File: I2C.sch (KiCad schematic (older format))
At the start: 2 parts, among them U1 PCA9306DP

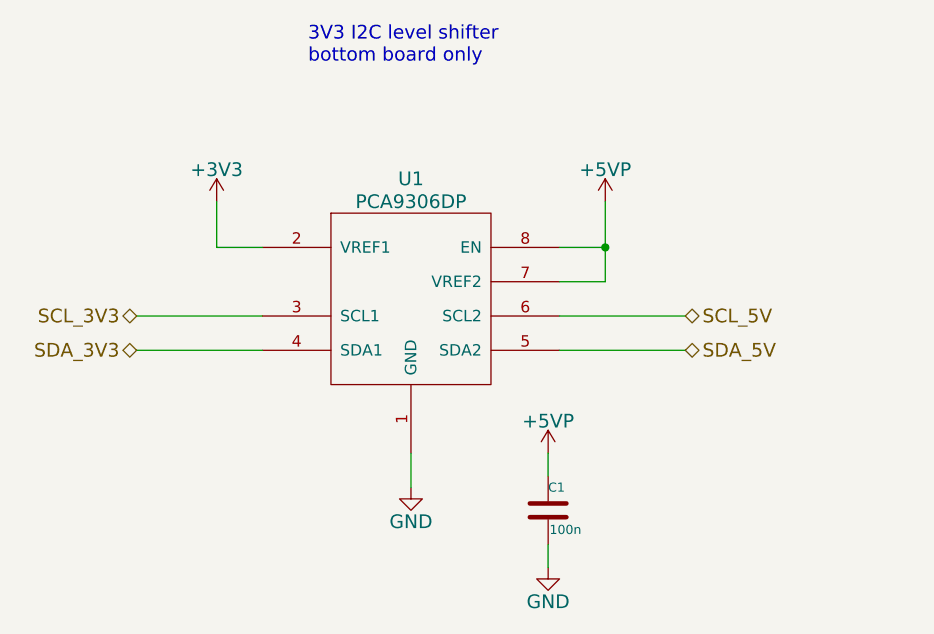
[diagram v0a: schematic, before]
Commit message: Added pullup resistors to I2C
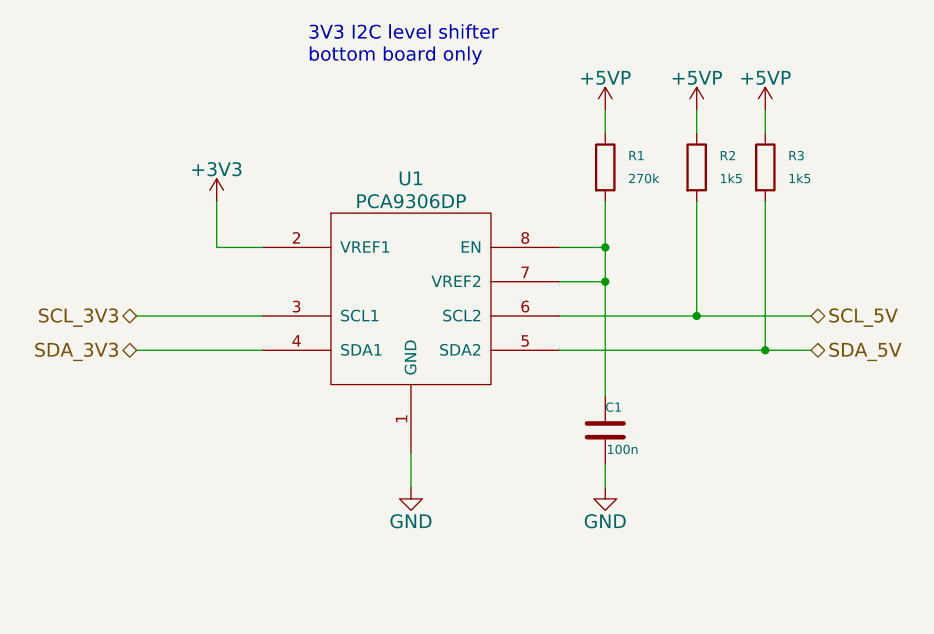
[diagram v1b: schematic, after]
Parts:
- added R1: 270k, Resistors_SMD:R_0805, symbol R
- added R2, R3: 1k5, Resistors_SMD:R_0805, symbol R
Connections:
- net +5VP: now also R1.1, R2.1, R3.1; no longer C1.1, U1.7 (VREF2), U1.8 (EN)
- net SCL_5V: now also R2.2
- net SDA_5V: now also R3.2
- new net: C1.1, R1.2, U1.7 (VREF2), U1.8 (EN)
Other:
- moved on the sheet: C1
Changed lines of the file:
@@
 	4000 2500 4000 2300
 $Comp
-L +3V3 #PWR010
+L +3V3 #PWR10
 U 1 1 54D96007
 P 4000 2300
-F 0 "#PWR010" H 4000 2150 60  0001 C CNN
+F 0 "#PWR10" H 4000 2150 60  0001 C CNN
 F 1 "+3V3" H 4000 2440 60  0000 C CNN
 F 2 "" H 4000 2300 60  0000 C CNN
@@
 	5700 2650 5500 2650
 Wire Wire Line
-	5700 2300 5700 2650
-Wire Wire Line
 	5500 2500 5700 2500
-Connection ~ 5700 2500
 $Comp
-L +5VP #PWR011
+L +5VP #PWR14
 U 1 1 54D96030
-P 5700 2300
-F 0 "#PWR011" H 5700 2150 60  0001 C CNN
-F 1 "+5VP" H 5700 2440 60  0000 C CNN
-F 2 "" H 5700 2300 60  0000 C CNN
-F 3 "" H 5700 2300 60  0000 C CNN
-	1    5700 2300
+P 6100 1900
+F 0 "#PWR14" H 6100 1750 60  0001 C CNN
+F 1 "+5VP" H 6100 2040 60  0000 C CNN
+F 2 "" H 6100 1900 60  0000 C CNN
+F 3 "" H 6100 1900 60  0000 C CNN
+	1    6100 1900
 	1    0    0    -1
 $EndComp
@@
 	4850 3400 4850 3550
 $Comp
-L GND #PWR012
+L GND #PWR11
 U 1 1 54D96055
 P 4850 3550
-F 0 "#PWR012" H 4850 3300 60  0001 C CNN
+F 0 "#PWR11" H 4850 3300 60  0001 C CNN
 F 1 "GND" H 4850 3400 60  0000 C CNN
 F 2 "" H 4850 3550 60  0000 C CNN
@@
 $EndComp
 $Comp
-L GND #PWR013
+L GND #PWR13
 U 1 1 54D9606F
-P 5450 3900
-F 0 "#PWR013" H 5450 3650 60  0001 C CNN
-F 1 "GND" H 5450 3750 60  0000 C CNN
-F 2 "" H 5450 3900 60  0000 C CNN
-F 3 "" H 5450 3900 60  0000 C CNN
-	1    5450 3900
+P 5700 3550
+F 0 "#PWR13" H 5700 3300 60  0001 C CNN
+F 1 "GND" H 5700 3400 60  0000 C CNN
+F 2 "" H 5700 3550 60  0000 C CNN
+F 3 "" H 5700 3550 60  0000 C CNN
+	1    5700 3550
 	1    0    0    -1
 $EndComp
@@
 L C C1
 U 1 1 54D96092
-P 5450 3650
-F 0 "C1" H 5450 3750 40  0000 L CNN
-F 1 "100n" H 5456 3565 40  0000 L CNN
-F 2 "Capacitors_SMD:C_0805" H 5488 3500 30  0001 C CNN
-F 3 "" H 5450 3650 60  0000 C CNN
-F 4 "MC0805B104K250CT" H 5450 3650 60  0001 C CNN "Part Number"
-F 5 "Multicomp" H 5450 3650 60  0001 C CNN "Manufacturer"
-F 6 "0805" H 5450 3650 60  0001 C CNN "Package"
-F 7 "Farnell" H 5450 3650 60  0001 C CNN "Supplier"
-F 8 "1759166" H 5450 3650 60  0001 C CNN "Order Code"
-F 9 "Mouser" H 5450 3650 60  0001 C CNN "Alt. Supplier"
-F 10 "710-885012207098" H 5450 3650 60  0001 C CNN "Alt. Order Code"
-F 11 "100nF/50V X7R 0805 ceramic capacitor" H 5450 3650 60  0001 C CNN "Note"
-	1    5450 3650
+P 5700 3300
+F 0 "C1" H 5700 3400 40  0000 L CNN
+F 1 "100n" H 5706 3215 40  0000 L CNN
+F 2 "Capacitors_SMD:C_0805" H 5738 3150 30  0001 C CNN
+F 3 "" H 5700 3300 60  0000 C CNN
+F 4 "MC0805B104K250CT" H 5700 3300 60  0001 C CNN "Part Number"
+F 5 "Multicomp" H 5700 3300 60  0001 C CNN "Manufacturer"
+F 6 "0805" H 5700 3300 60  0001 C CNN "Package"
+F 7 "Farnell" H 5700 3300 60  0001 C CNN "Supplier"
+F 8 "1759166" H 5700 3300 60  0001 C CNN "Order Code"
+F 9 "Mouser" H 5700 3300 60  0001 C CNN "Alt. Supplier"
+F 10 "710-885012207098" H 5700 3300 60  0001 C CNN "Alt. Order Code"
+F 11 "100nF/50V X7R 0805 ceramic capacitor" H 5700 3300 60  0001 C CNN "Note"
+	1    5700 3300
 	1    0    0    -1
 $EndComp
 Wire Wire Line
-	5450 3500 5450 3400
+	5700 3550 5700 3450
 Wire Wire Line
-	5450 3900 5450 3800
-$Comp
-L +5VP #PWR014
-U 1 1 54D960F9
-P 5450 3400
-F 0 "#PWR014" H 5450 3250 60  0001 C CNN
-F 1 "+5VP" H 5450 3540 60  0000 C CNN
-F 2 "" H 5450 3400 60  0000 C CNN
-F 3 "" H 5450 3400 60  0000 C CNN
-	1    5450 3400
-	1    0    0    -1
-$EndComp
+	5500 2800 6600 2800
 Wire Wire Line
-	5500 2800 6050 2800
-Wire Wire Line
-	5500 2950 6050 2950
+	5500 2950 6600 2950
 Wire Wire Line
 	4200 2800 3650 2800
@@
 Text HLabel 3650 2950 0    60   BiDi ~ 0
 SDA_3V3
-Text HLabel 6050 2800 2    60   BiDi ~ 0
+Text HLabel 6600 2800 2    60   BiDi ~ 0
 SCL_5V
-Text HLabel 6050 2950 2    60   BiDi ~ 0
+Text HLabel 6600 2950 2    60   BiDi ~ 0
 SDA_5V
 Text Notes 4400 1700 0    60   ~ 0
 3V3 I2C level shifter\nbottom board only
+$Comp
+L R R1
+U 1 1 56EC1C2A
+P 5700 2150
+F 0 "R1" H 5800 2200 40  0000 L CNN
+F 1 "270k" H 5800 2100 40  0000 L CNN
+F 2 "Resistors_SMD:R_0805" V 5630 2150 30  0001 C CNN
+F 3 "" H 5700 2150 30  0000 C CNN
+F 4 "MCSR08X2703FTL" V 5700 2150 60  0001 C CNN "Part Number"
+F 5 "Multicomp" V 5700 2150 60  0001 C CNN "Manufacturer"
+F 6 "0805" H 5700 2150 60  0001 C CNN "Package"
+F 7 "Farnell" H 5700 2150 60  0001 C CNN "Supplier"
+F 8 "2074426" V 5700 2150 60  0001 C CNN "Order Code"
+F 9 "Mouser" H 5700 2150 60  0001 C CNN "Alt. Supplier"
+F 10 "ERJ-6ENF2703V" H 5700 2150 60  0001 C CNN "Alt. Order Code"
+F 11 "270kΩ/1% 0805 resistor" H 5700 2150 60  0001 C CNN "Note"
+	1    5700 2150
+	1    0    0    -1
+$EndComp
+Wire Wire Line
+	6100 1900 6100 2000
+Wire Wire Line
+	5700 2300 5700 3150
+Connection ~ 5700 2500
+Connection ~ 5700 2650
+$Comp
+L R R2
+U 1 1 56EC20D7
+P 6100 2150
+F 0 "R2" H 6200 2200 40  0000 L CNN
+F 1 "1k5" H 6200 2100 40  0000 L CNN
+F 2 "Resistors_SMD:R_0805" V 6030 2150 30  0001 C CNN
+F 3 "" H 6100 2150 30  0000 C CNN
+F 4 "MCWR08X1501FTL" V 6100 2150 60  0001 C CNN "Part Number"
+F 5 "Multicomp" V 6100 2150 60  0001 C CNN "Manufacturer"
+F 6 "0805" H 6100 2150 60  0001 C CNN "Package"
+F 7 "Farnell" H 6100 2150 60  0001 C CNN "Supplier"
+F 8 "2447592" V 6100 2150 60  0001 C CNN "Order Code"
+F 9 "Mouser" H 6100 2150 60  0001 C CNN "Alt. Supplier"
+F 10 "71-CRCW0805-1.5K-E3" H 6100 2150 60  0001 C CNN "Alt. Order Code"
+F 11 "1.5kΩ/1% 0805 resistor" H 6100 2150 60  0001 C CNN "Note"
+	1    6100 2150
+	1    0    0    -1
+$EndComp
+$Comp
+L R R3
+U 1 1 56EC2261
+P 6400 2150
+F 0 "R3" H 6500 2200 40  0000 L CNN
+F 1 "1k5" H 6500 2100 40  0000 L CNN
+F 2 "Resistors_SMD:R_0805" V 6330 2150 30  0001 C CNN
+F 3 "" H 6400 2150 30  0000 C CNN
+F 4 "MCWR08X1501FTL" V 6400 2150 60  0001 C CNN "Part Number"
+F 5 "Multicomp" V 6400 2150 60  0001 C CNN "Manufacturer"
+F 6 "0805" H 6400 2150 60  0001 C CNN "Package"
+F 7 "Farnell" H 6400 2150 60  0001 C CNN "Supplier"
+F 8 "2447592" V 6400 2150 60  0001 C CNN "Order Code"
+F 9 "Mouser" H 6400 2150 60  0001 C CNN "Alt. Supplier"
+F 10 "71-CRCW0805-1.5K-E3" H 6400 2150 60  0001 C CNN "Alt. Order Code"
+F 11 "1.5kΩ/1% 0805 resistor" H 6400 2150 60  0001 C CNN "Note"
+	1    6400 2150
+	1    0    0    -1
+$EndComp
+Wire Wire Line
+	6100 2300 6100 2800
+Connection ~ 6100 2800
+Wire Wire Line
+	6400 2300 6400 2950
+Connection ~ 6400 2950
+$Comp
+L +5VP #PWR12
+U 1 1 56EC22D8
+P 5700 1900
+F 0 "#PWR12" H 5700 1750 60  0001 C CNN
+F 1 "+5VP" H 5700 2040 60  0000 C CNN
+F 2 "" H 5700 1900 60  0000 C CNN
+F 3 "" H 5700 1900 60  0000 C CNN
+	1    5700 1900
+	1    0    0    -1
+$EndComp
+Wire Wire Line
+	5700 1900 5700 2000
+$Comp
+L +5VP #PWR15
+U 1 1 56EC22EB
+P 6400 1900
+F 0 "#PWR15" H 6400 1750 60  0001 C CNN
+F 1 "+5VP" H 6400 2040 60  0000 C CNN
+F 2 "" H 6400 1900 60  0000 C CNN
+F 3 "" H 6400 1900 60  0000 C CNN
+	1    6400 1900
+	1    0    0    -1
+$EndComp
+Wire Wire Line
+	6400 1900 6400 2000
 $EndSCHEMATC

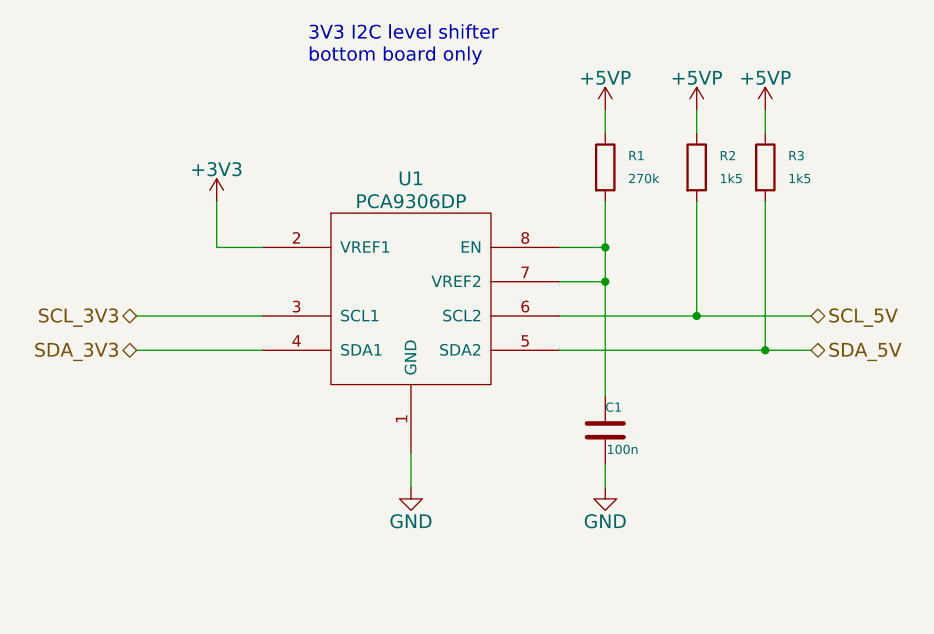
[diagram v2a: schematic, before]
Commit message: Changed 100n->100p capacitor on the I2C level shifter
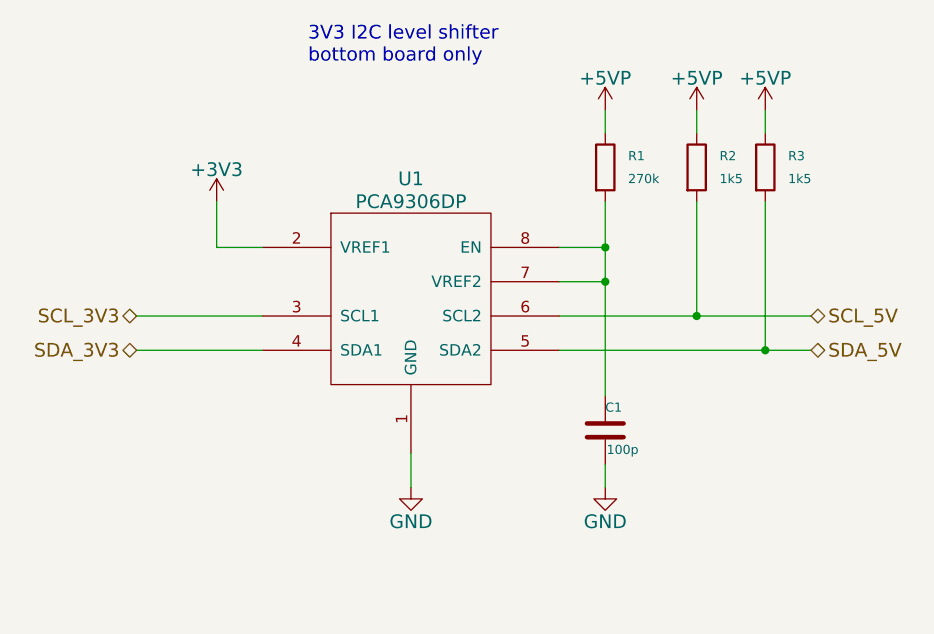
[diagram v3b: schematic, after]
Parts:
- C1: value 100n -> 100p; Alt. Order Code 710-885012207098 -> 810-CGA4C2C0G2A101J; Manufacturer Multicomp -> TDK; Note 100nF/50V X7R 0805 ceramic capacitor -> 100pF/100V C0G(NP0) 0805 ceramic capacitor; Order Code 1759166 -> 2210931; Part Number MC0805B104K250CT -> CGA4C2C0G2A101J060AA
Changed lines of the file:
@@
 P 5700 3300
 F 0 "C1" H 5700 3400 40  0000 L CNN
-F 1 "100n" H 5706 3215 40  0000 L CNN
+F 1 "100p" H 5706 3215 40  0000 L CNN
 F 2 "Capacitors_SMD:C_0805" H 5738 3150 30  0001 C CNN
 F 3 "" H 5700 3300 60  0000 C CNN
-F 4 "MC0805B104K250CT" H 5700 3300 60  0001 C CNN "Part Number"
-F 5 "Multicomp" H 5700 3300 60  0001 C CNN "Manufacturer"
+F 4 "CGA4C2C0G2A101J060AA" H 5700 3300 60  0001 C CNN "Part Number"
+F 5 "TDK" H 5700 3300 60  0001 C CNN "Manufacturer"
 F 6 "0805" H 5700 3300 60  0001 C CNN "Package"
 F 7 "Farnell" H 5700 3300 60  0001 C CNN "Supplier"
-F 8 "1759166" H 5700 3300 60  0001 C CNN "Order Code"
+F 8 "2210931" H 5700 3300 60  0001 C CNN "Order Code"
 F 9 "Mouser" H 5700 3300 60  0001 C CNN "Alt. Supplier"
-F 10 "710-885012207098" H 5700 3300 60  0001 C CNN "Alt. Order Code"
-F 11 "100nF/50V X7R 0805 ceramic capacitor" H 5700 3300 60  0001 C CNN "Note"
+F 10 "810-CGA4C2C0G2A101J" H 5700 3300 60  0001 C CNN "Alt. Order Code"
+F 11 "100pF/100V C0G(NP0) 0805 ceramic capacitor" H 5700 3300 60  0001 C CNN "Note"
 	1    5700 3300
 	1    0    0    -1
